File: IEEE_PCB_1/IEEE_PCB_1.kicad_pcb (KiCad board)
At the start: 2 copper layers, 89.3 x 109 mm, 18 parts, among them U1 555, U2 4017, U3 EG1218, U4 1058TR

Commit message: silkscreen outline in progress
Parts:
- added REF**: decorball, OrnamentOutlines:decorball, F.Cu at (0.00, 0.00)

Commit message: same
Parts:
- moved REF** 291.1 mm to (276.8, 90.2)

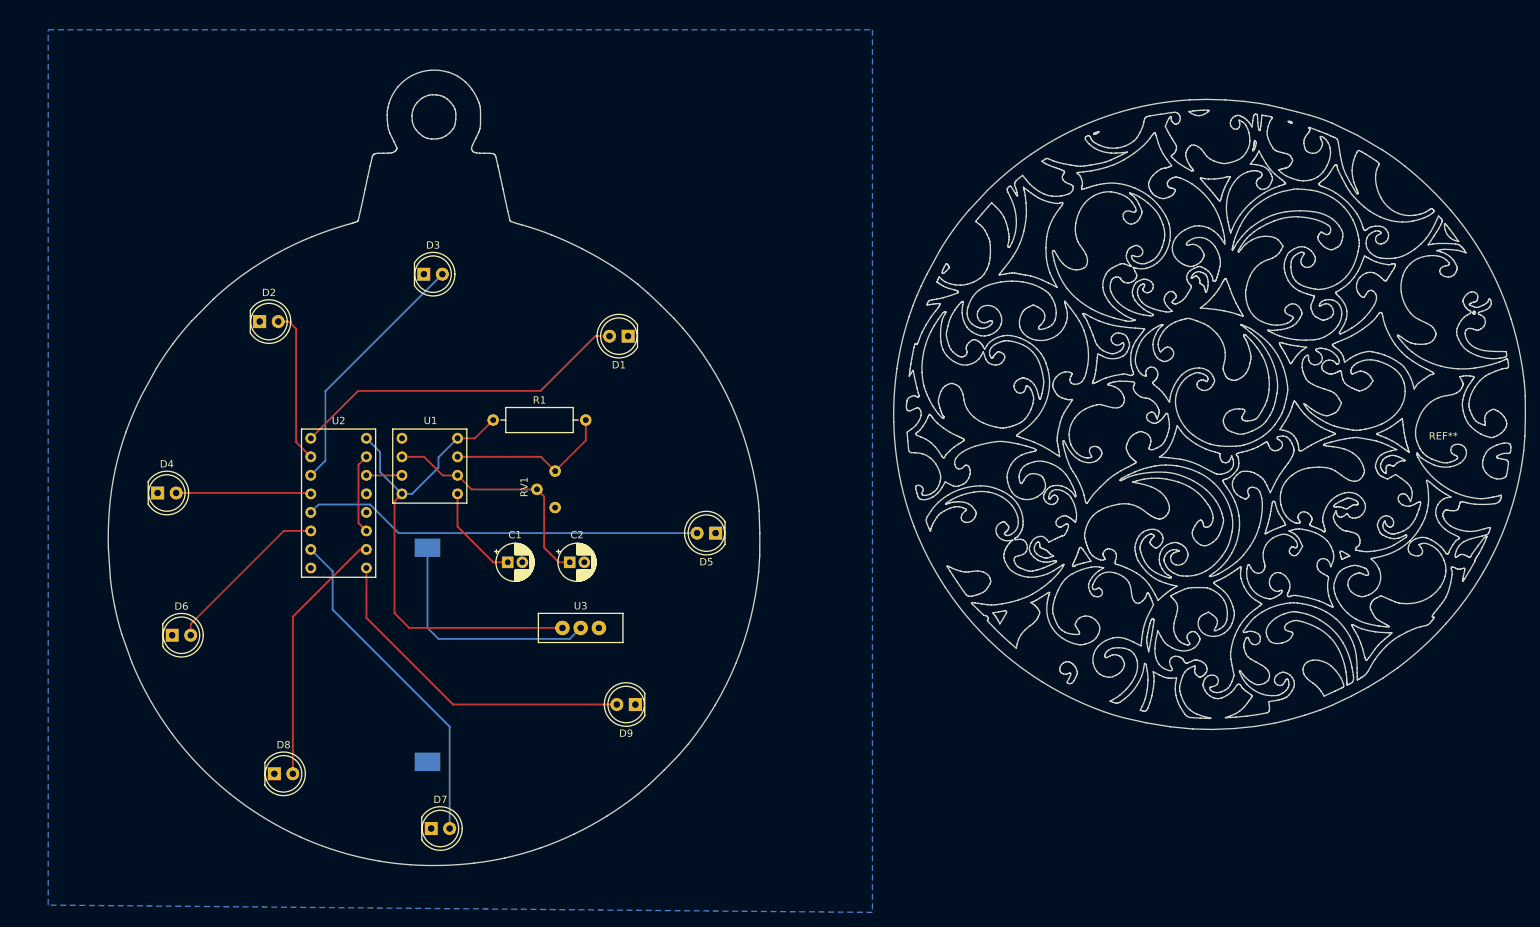
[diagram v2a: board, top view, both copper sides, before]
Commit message: Rev5
new ball ornament design
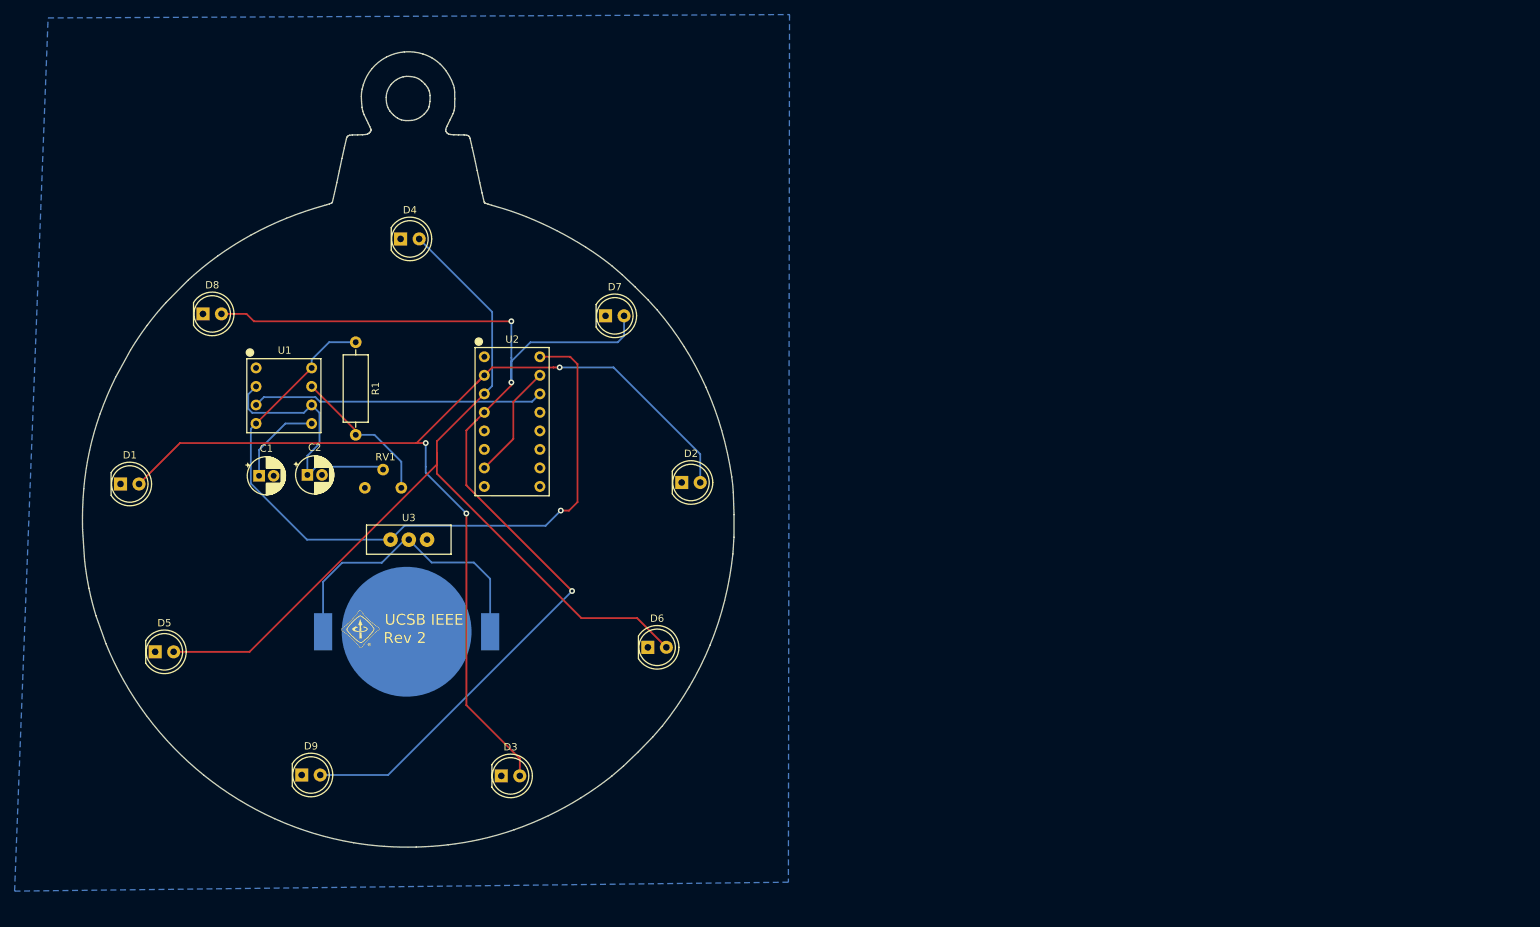
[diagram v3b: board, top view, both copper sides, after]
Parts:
- removed ?: , 
- removed the REF** at (276.8, 90.2)
- added G***: LOGO, Logos:IEEE Logo, F.Cu at (128.3, 117.2)
- added REF**: BallOrnament, OrnamentOutlines:BallOrnament, F.Cu at (132.2, 107.5)
- D1, D2, D3: value LED -> YELLOW
- D4, D5, D6, D7, D8, D9: value LED -> RED
- RV1: value R_POT_US -> 50K
- U4: value 1058TR -> CR2025TR; footprint IEEE_PCB_Ornament:1058TR -> IEEE_PCB_Ornament:CR2025TR
- moved D5 78.5 mm to (100.2, 120.3), turned to 0 degrees
- moved D7 74.2 mm to (161.9, 74.2)
- moved D1 72.5 mm to (95.4, 97.3), turned to 0 degrees
- moved D3 69.6 mm to (147.6, 137.3)
- moved D6 65.2 mm to (167.7, 119.7)
- moved D8 63.8 mm to (106.7, 73.9)
- moved D2 61.9 mm to (172.3, 97.1)
- moved D4 48.2 mm to (133.8, 63.7)
- moved D9 46.8 mm to (120.3, 137.2), turned to 0 degrees
- moved C2 37.9 mm to (121.0, 96.0)
- moved C1 36.1 mm to (114.4, 96.1)
- moved U3 26.5 mm to (134.9, 104.9)
- moved U2 26.3 mm to (145.3, 79.8)
- moved RV1 23.6 mm to (131.4, 97.8), turned to 0 degrees
- moved U1 22.2 mm to (114.0, 81.4)
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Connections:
- D2 pad 2: Net-(D2-Pad2) -> Net-(D1-Pad2)
- D3 pad 2: Net-(D3-Pad2) -> Net-(D1-Pad2)
- D5 pad 2: Net-(D5-Pad2) -> Net-(D4-Pad2)
- D6 pad 2: Net-(D6-Pad2) -> Net-(D4-Pad2)
- D8 pad 2: Net-(D8-Pad2) -> Net-(D7-Pad2)
- D9 pad 2: Net-(D9-Pad2) -> Net-(D7-Pad2)
- U2 pad 1: Net-(D1-Pad2) -> Net-(U2-Pad1)
- U2 pad 10: Net-(D8-Pad2) -> Net-(U2-Pad10)
- U2 pad 15: Net-(U2-Pad11) -> Net-(U2-Pad15)
- U2 pad 2: Net-(D2-Pad2) -> Net-(D1-Pad2)
- U2 pad 3: Net-(D3-Pad2) -> Net-(D4-Pad2)
- U2 pad 4: Net-(D4-Pad2) -> Net-(D7-Pad2)
- U2 pad 5: Net-(D5-Pad2) -> Net-(U2-Pad5)
- U2 pad 6: Net-(D6-Pad2) -> Net-(U2-Pad6)
- U2 pad 7: Net-(D7-Pad2) -> Net-(U2-Pad15)
- U2 pad 9: Net-(D9-Pad2) -> Net-(U2-Pad9)
- U3 pad 3: GND -> Net-(U3-Pad3)
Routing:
- net Net-(D4-Pad2): track 18.5 -> 129.0 mm
- net Net-(D7-Pad2): track 46.1 -> 153.2 mm, vias 0 -> 3
- net Net-(D1-Pad2): track 46.8 -> 146.1 mm, vias 0 -> 3
- net Net-(D5-Pad2): track 55.0 -> 0.00 mm
- net Net-(D9-Pad2): track 46.1 -> 0.00 mm
- net Net-(D8-Pad2): track 35.4 -> 0.00 mm
- net Signal: track 4.88 -> 40.1 mm
- net Net-(D3-Pad2): track 35.1 -> 0.00 mm
- net +3V3: track 68.5 -> 102.1 mm, vias 0 -> 1
- net Net-(D6-Pad2): track 23.3 -> 0.00 mm
- net Net-(D2-Pad2): track 21.2 -> 0.00 mm
- net Net-(U2-Pad15): track 0.00 -> 15.9 mm
- net Net-(U2-Pad11): track 11.1 -> 0.00 mm
- net Net-(U3-Pad2): track 33.2 -> 41.6 mm
- net Net-(R1-Pad2): track 22.9 -> 20.5 mm
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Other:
- board text added: "Rev 2"
- board text added: "UCSB IEEE"

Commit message: changed silkscreen
forgot to push
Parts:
- added G***: LOGO, LOGO, F.Cu at (134.9, 92.8)
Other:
- net class Default removed
